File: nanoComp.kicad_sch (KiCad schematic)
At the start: 21 parts, among them J1 USB_C_Receptacle_PowerOnly_6P, J2 USB_A, J3 USB_A, J4 Conn_01x06_Pin, J5 Conn_01x14, J6 Conn_01x04, SW1 SW_Wuerth_450301014042

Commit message: Finishing touches + manufacturing files
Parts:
- removed D1: 1N5819WS, Diode_SMD:D_SOD-323_HandSoldering, symbol Diode:1N5819WS
- added D1: 1N5819HW-7-F, Diode_SMD:D_SOD-123, symbol nanoComp:1N5819HW-7-F
- C1: Manufacturer (none) -> Generic; Supplier (none) -> Mouser; Supplier P/N (none) -> 603-CC805KKX7R7BB105
- D2: Manufacturer (none) -> Bivar; Manufacturer P/N (none) -> SM0805UGC; Supplier (none) -> Mouser; Supplier P/N (none) -> 749-SM0805UGC
- J1: Manufacturer (none) -> GCT; Manufacturer P/N (none) -> USB4125-GF-A; Supplier (none) -> Mouser; Supplier P/N (none) -> 640-USB4125-GF-A
- J2, J3: Manufacturer (none) -> Molex; Manufacturer P/N (none) -> 67643-3910; Supplier (none) -> Mouser; Supplier P/N (none) -> 538-67643-3910
- J4: Manufacturer (none) -> Generic; Supplier (none) -> Mouser; Supplier P/N (none) -> 855-M20-9990646
- J5: Manufacturer (none) -> Generic; Supplier (none) -> Mouser; Supplier P/N (none) -> 538-22-28-4146
- J6: Manufacturer (none) -> Generic; Supplier (none) -> Mouser; Supplier P/N (none) -> 538-22-28-4042
- R1, R2: Manufacturer (none) -> Generic; Supplier (none) -> Mouser; Supplier P/N (none) -> 594-MCU08050C5101FP5
- R3: Manufacturer (none) -> Generic; Supplier (none) -> Mouser; Supplier P/N (none) -> 71-TNPW08051K00FEEA
- R4, R5, R6: now not fitted
- SW1: Manufacturer (none) -> Wurth; Manufacturer P/N (none) -> 450301014042; Supplier (none) -> Mouser; Supplier P/N (none) -> 710-450301014042
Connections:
- net at C1.1, SW1.1 (B): now also D1.1 (K)
- net at J1.A9 (VBUS), J1.B9 (VBUS): now also D1.2 (A)

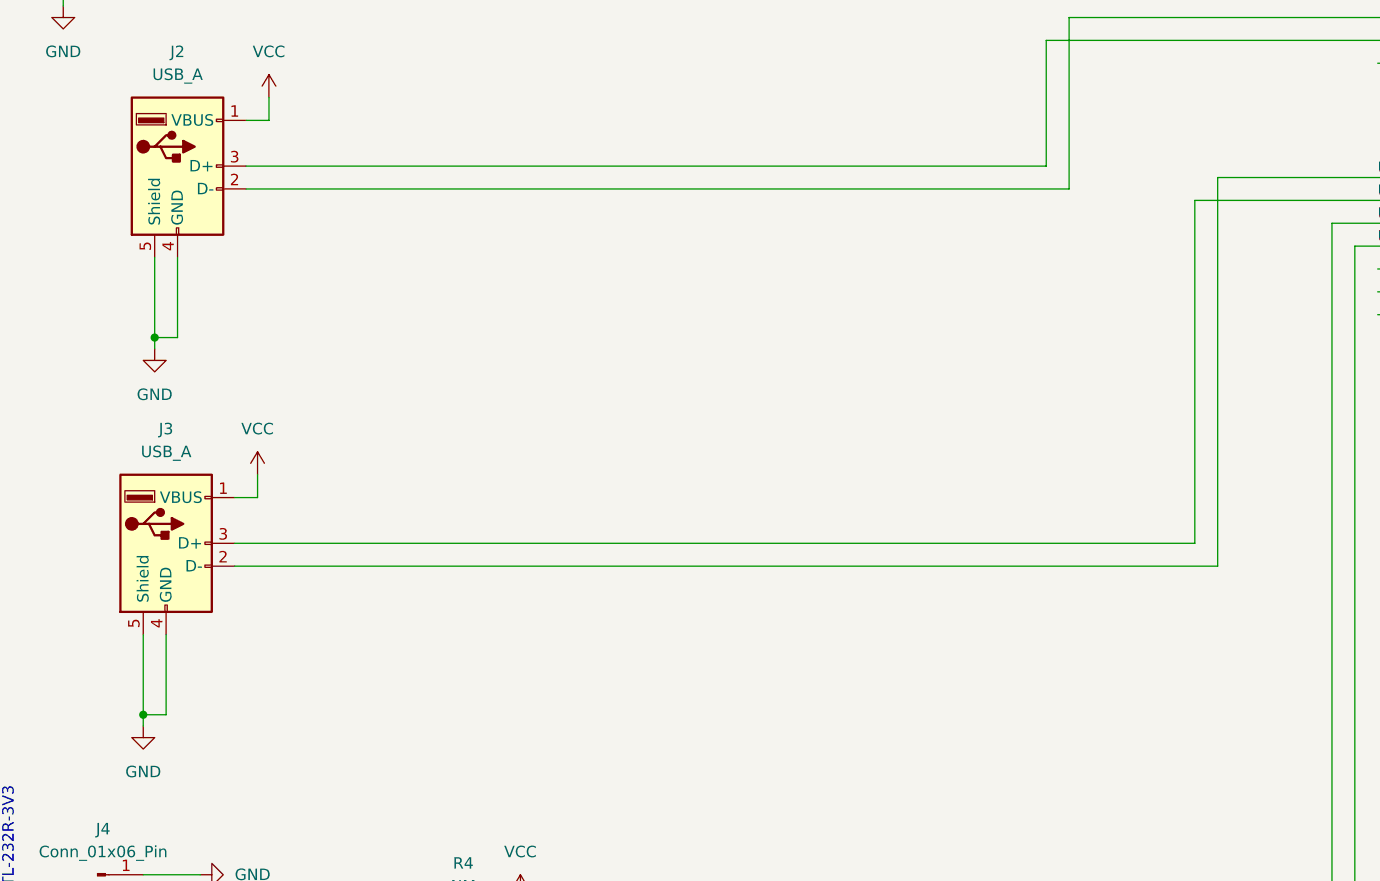
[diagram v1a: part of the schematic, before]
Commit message: Added 15k pulldowns on USB data lines for master configuration
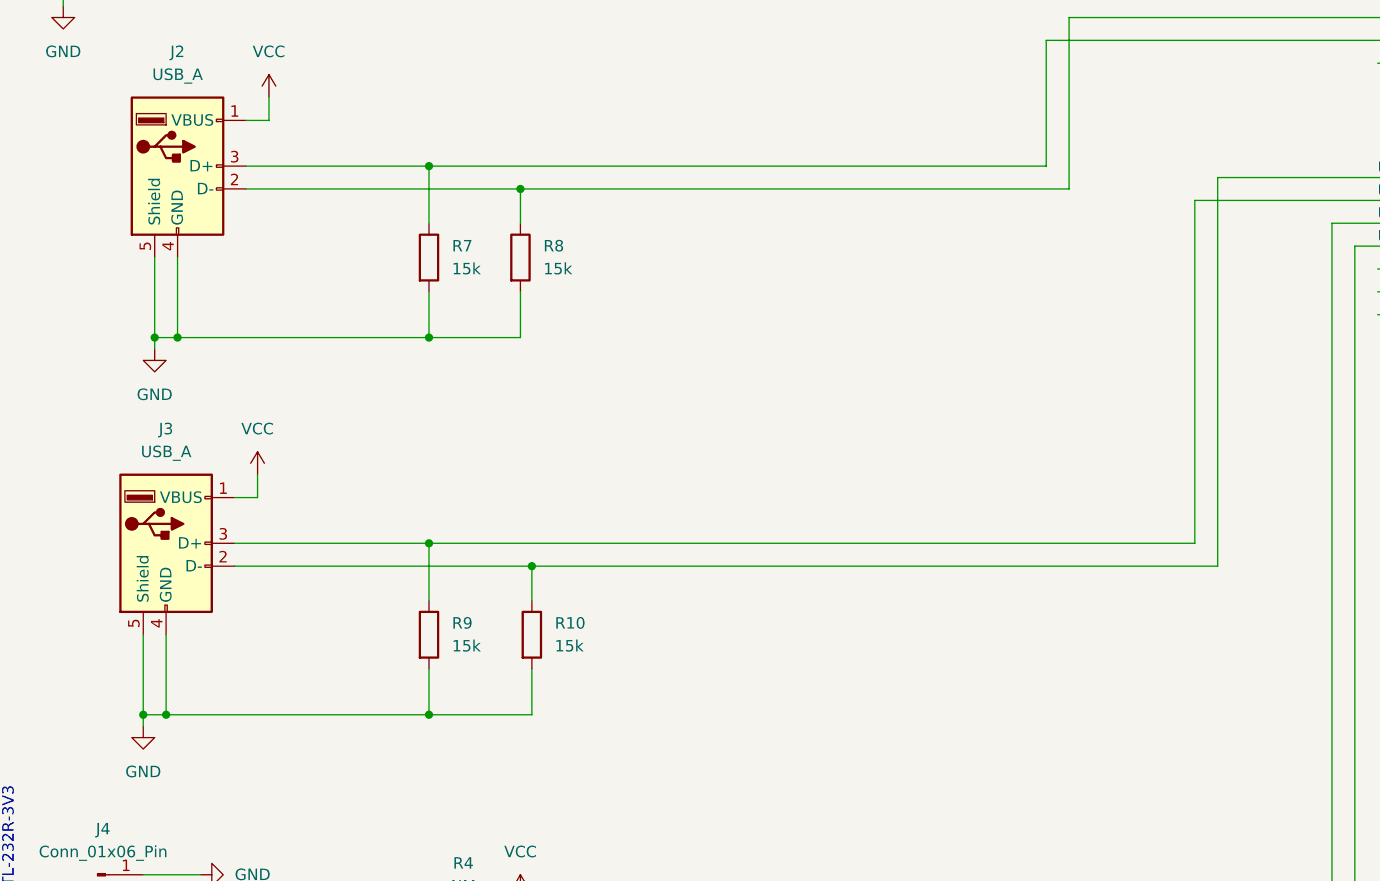
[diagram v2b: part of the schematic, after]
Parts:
- added R10, R7, R8, R9: 15k, Resistor_SMD:R_0805_2012Metric, symbol Device:R
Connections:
- net GND: now also R10.2, R7.2, R8.2, R9.2
- net USB_A_D+: now also R7.1
- net USB_A_D-: now also R8.1
- net USB_B_D+: now also R9.1
- net USB_B_D-: now also R10.1
